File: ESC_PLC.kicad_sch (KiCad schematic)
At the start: 0 parts

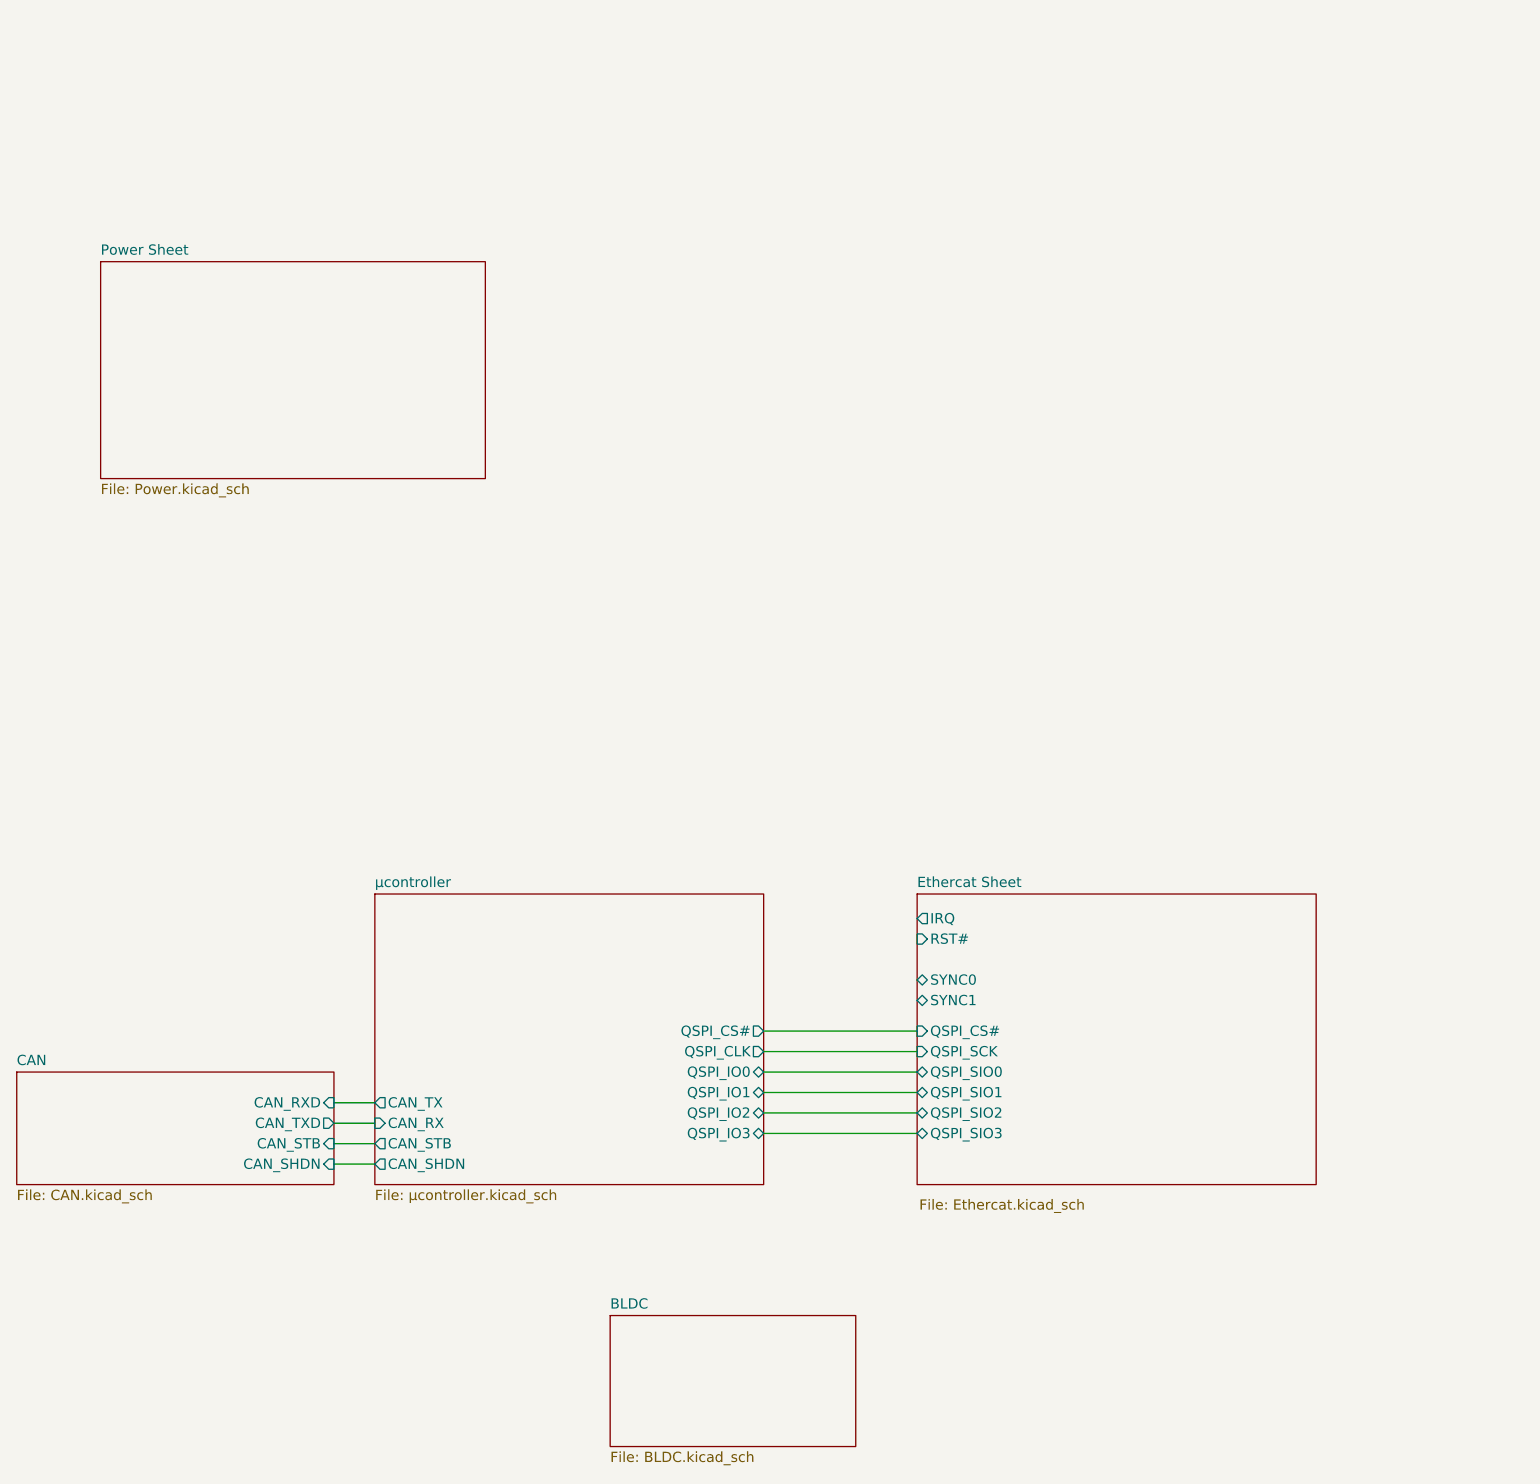
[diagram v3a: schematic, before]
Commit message: BLDC en 5V
bldc motor aangesloten alsook 5V gemaakt
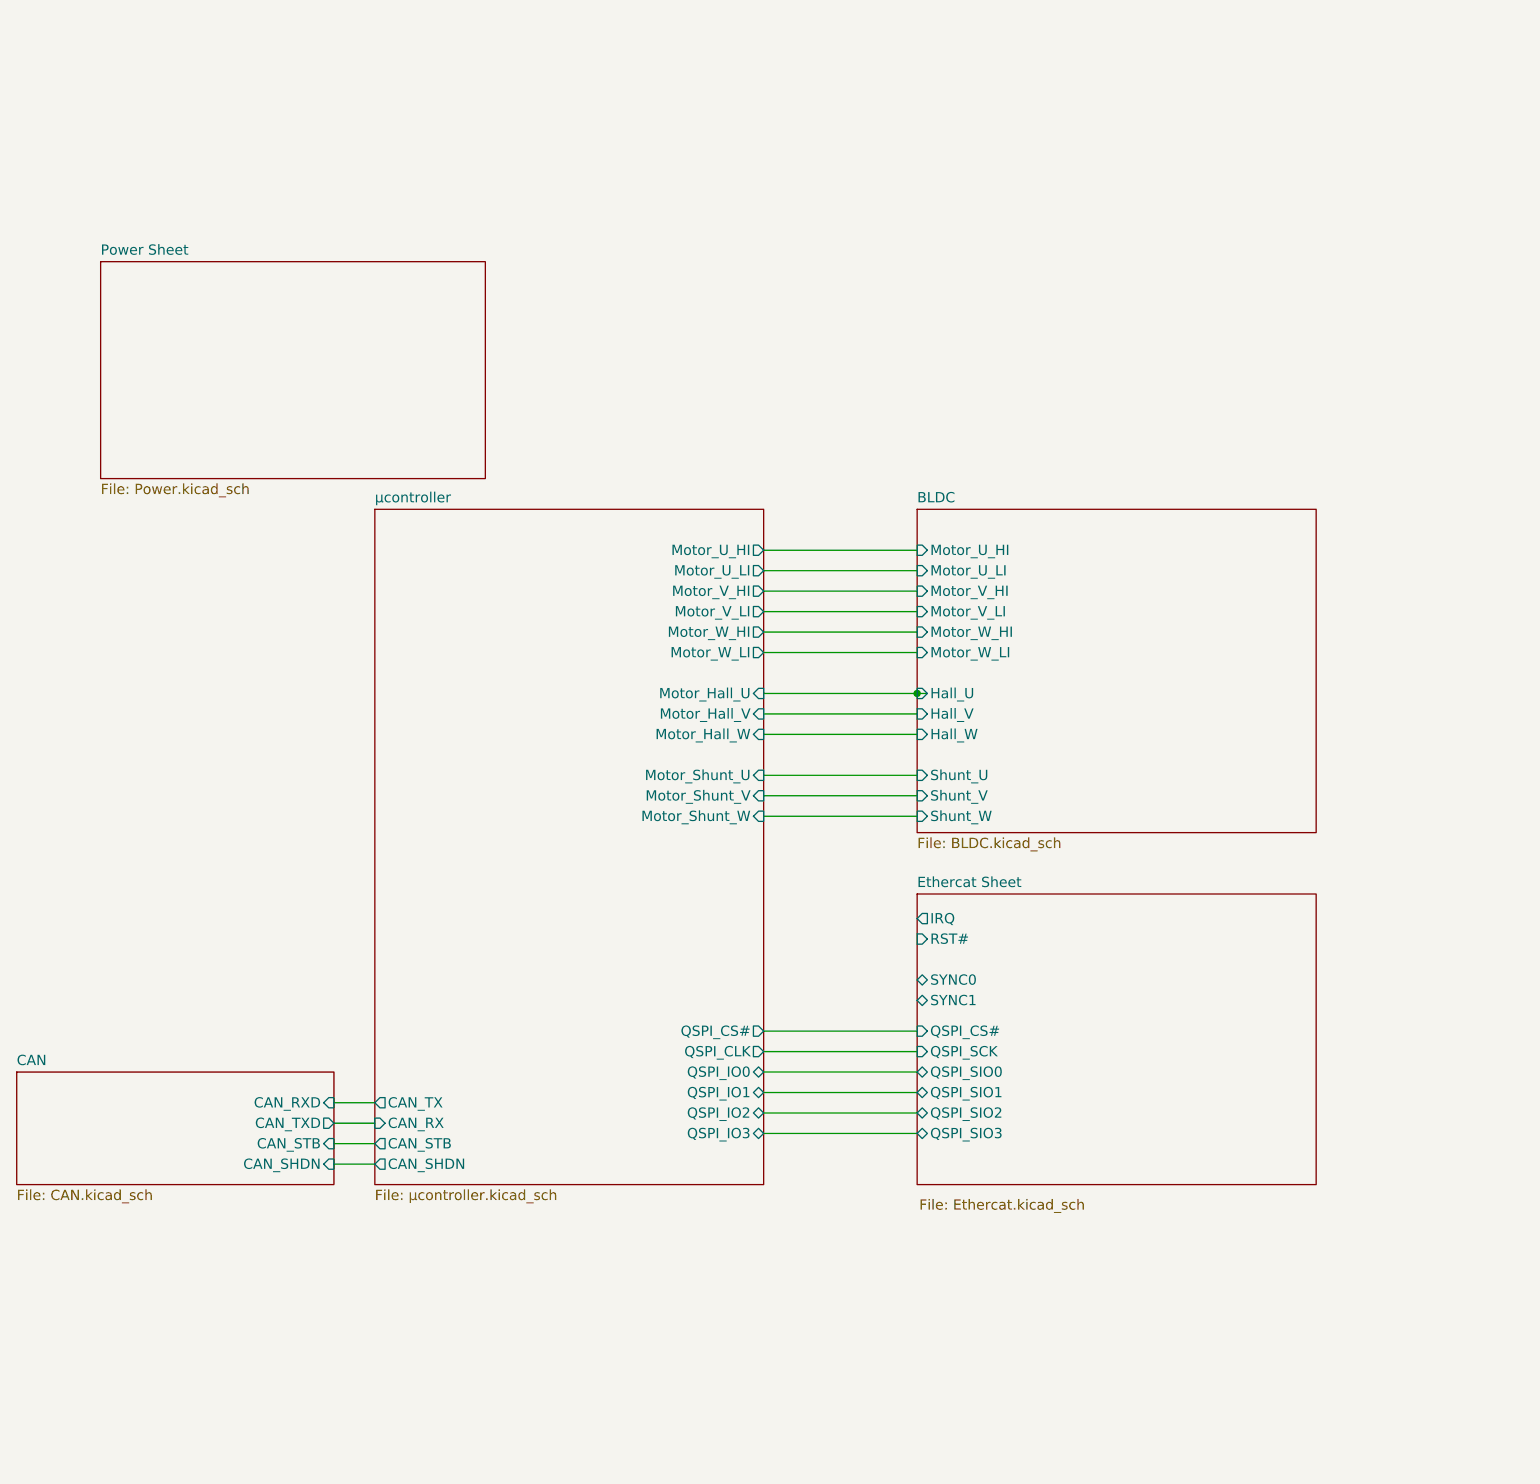
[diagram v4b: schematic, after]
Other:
- sheet BLDC ports: added Hall_U, Hall_V, Hall_W, Motor_U_HI, Motor_U_LI, Motor_V_HI, Motor_V_LI, Motor_W_HI, Motor_W_LI, Shunt_U, Shunt_V, Shunt_W; removed none
- sheet µcontroller ports: added Motor_Hall_U, Motor_Hall_V, Motor_Hall_W, Motor_Shunt_U, Motor_Shunt_V, Motor_Shunt_W, Motor_U_HI, Motor_U_LI, Motor_V_HI, Motor_V_LI, Motor_W_HI, Motor_W_LI; removed none

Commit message: schema's finalized
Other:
- sheet Ethercat Sheet ports: added none; removed RST#
- sheet µcontroller ports: added Ethercat_IRQ, Ethercat_Sync0, Ethercat_Sync1; removed none
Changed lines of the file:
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@@
+	(wire
+		(pts
+			(xy 135.89 151.13) (xy 154.94 151.13)
+		)
+		(stroke
+			(width 0)
+			(type default)
+		)
+	)
 	(wire
 		(pts
@@
 	(wire
 		(pts
+			(xy 135.89 148.59) (xy 154.94 148.59)
+		)
+		(stroke
+			(width 0)
+			(type default)
+		)
+	)
+	(wire
+		(pts
 			(xy 82.55 166.37) (xy 87.63 166.37)
 		)
@@
 		(pts
 			(xy 135.89 115.57) (xy 154.94 115.57)
+		)
+		(stroke
+			(width 0)
+			(type default)
+		)
+	)
+	(wire
+		(pts
+			(xy 135.89 153.67) (xy 154.94 153.67)
 		)
 		(stroke
@@
 			)
 		)
+		(pin "Ethercat_IRQ" input
+			(at 135.89 148.59 0)
+			(effects
+				(font
+					(size 1.27 1.27)
+				)
+				(justify right)
+			)
+		)
+		(pin "Ethercat_Sync0" bidirectional
+			(at 135.89 151.13 0)
+			(effects
+				(font
+					(size 1.27 1.27)
+				)
+				(justify right)
+			)
+		)
+		(pin "Ethercat_Sync1" bidirectional
+			(at 135.89 153.67 0)
+			(effects
+				(font
+					(size 1.27 1.27)
+				)
+				(justify right)
+			)
+		)
 		(instances
 			(project "ESC_PLC"
@@
 	)
 	(sheet
-		(at 154.94 140.462)
-		(size 49.53 36.068)
+		(at 154.94 144.78)
+		(size 49.53 31.75)
 		(exclude_from_sim no)
 		(in_bom yes)
@@
 		)
 		(property "Sheetname" "Ethercat Sheet"
-			(at 154.94 139.7504 0)
+			(at 154.94 144.0684 0)
 			(show_name no)
 			(do_not_autoplace no)
@@
 		)
 		(property "Sheetfile" "Ethercat.kicad_sch"
-			(at 155.194 178.308 0)
+			(at 154.813 177.927 0)
 			(show_name no)
 			(do_not_autoplace no)
@@
 			)
 		)
-		(pin "RST#" input
-			(at 154.94 146.05 180)
-			(effects
-				(font
-					(size 1.27 1.27)
-				)
-				(justify left)
-			)
-		)
 		(pin "SYNC0" bidirectional
 			(at 154.94 151.13 180)
@@
 		)
 		(pin "IRQ" output
-			(at 154.94 143.51 180)
-			(effects
-				(font
+			(at 154.94 148.59 180)
+			(effects
+				(font
